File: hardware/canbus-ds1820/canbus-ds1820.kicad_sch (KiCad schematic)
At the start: 35 parts, among them J1 USB_B_Micro, J2 SWD, J3 UART, J4 3-pole terminal, J5 CANBus, J6 CANBus, Q1 2N7002, Q2 2N7002, Q3 BSS84, U1 MCP1754S-3302xCB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

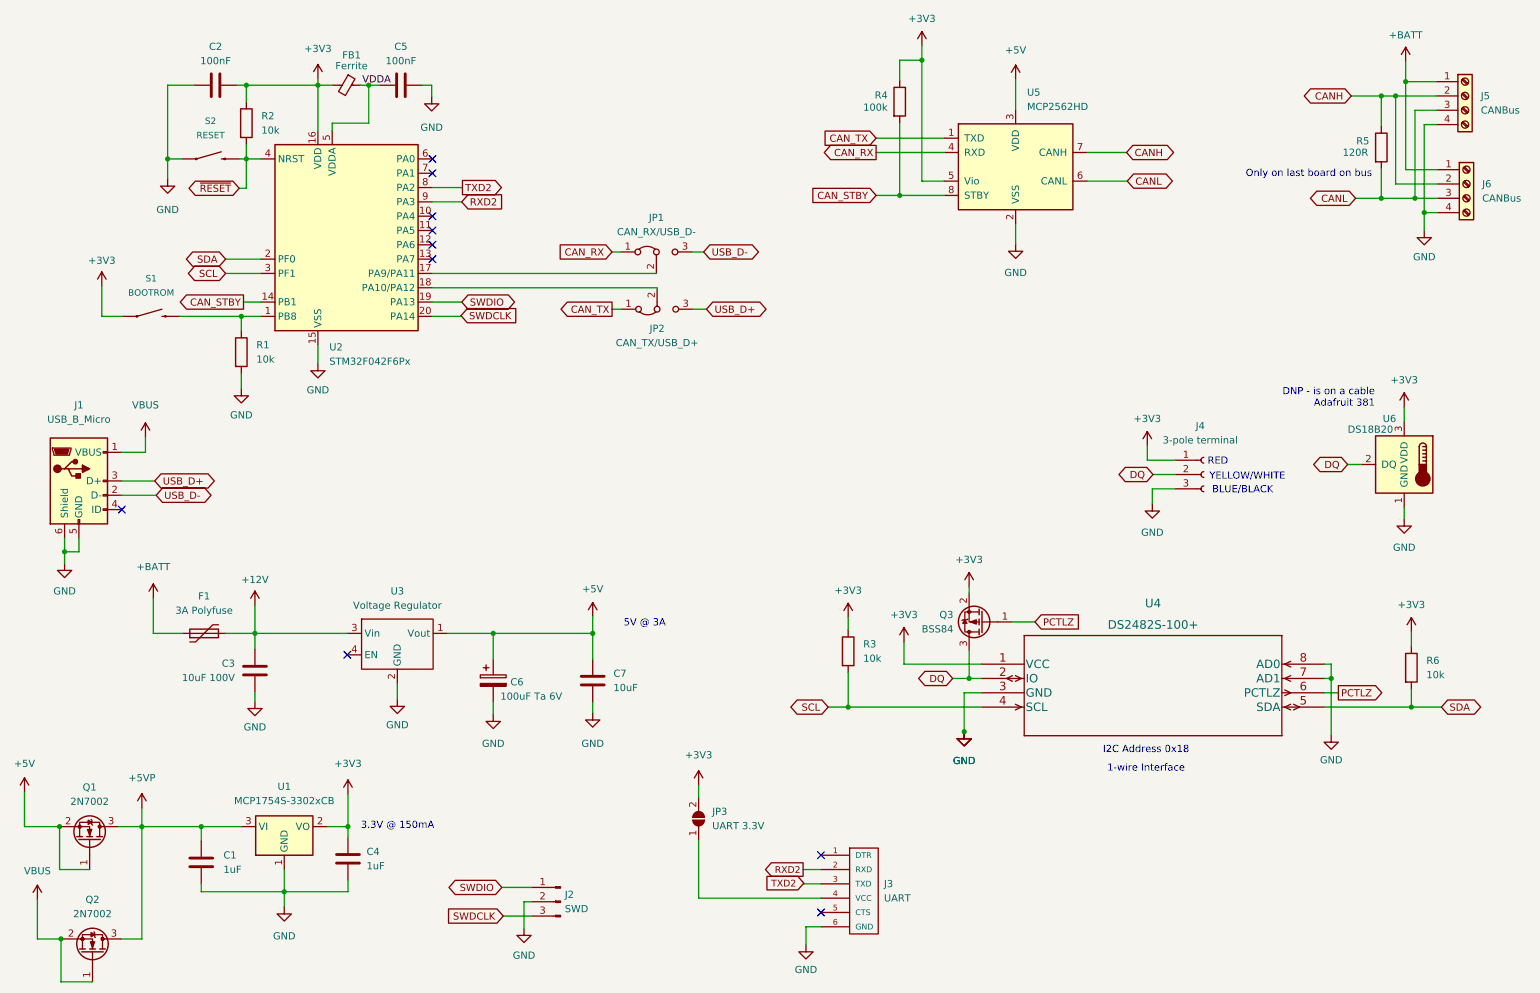
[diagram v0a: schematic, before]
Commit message: Implemented DS1820 directly, no DS2482
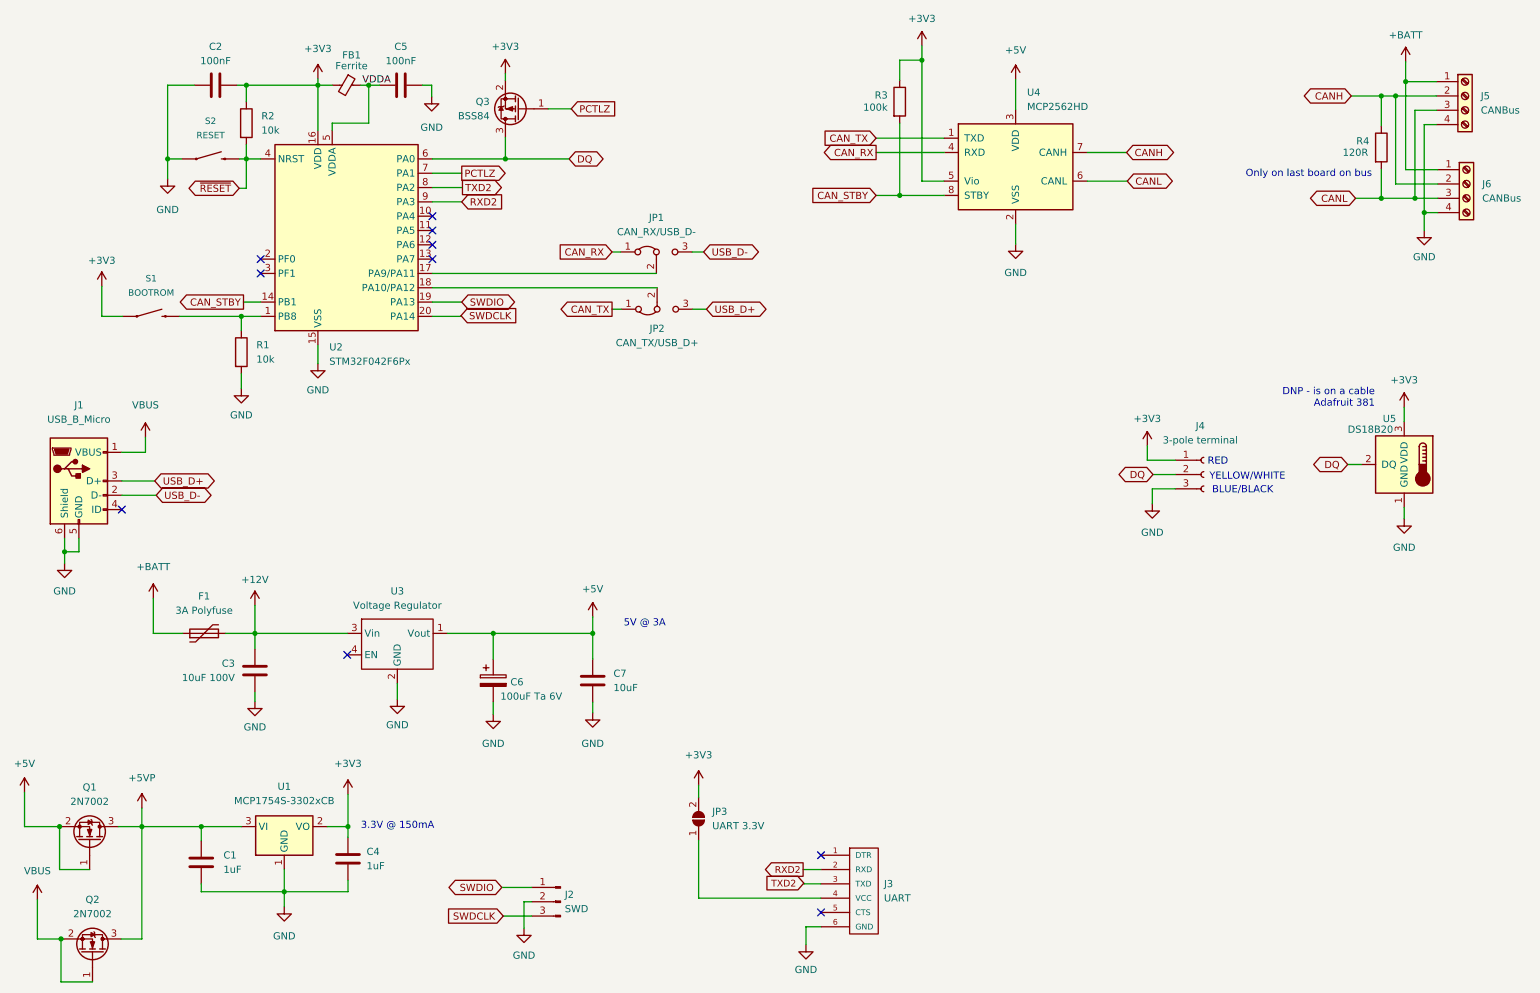
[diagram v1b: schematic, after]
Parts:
- removed R3, R6: 10k, Resistor_SMD:R_0805_2012Metric_Pad1.20x1.40mm_HandSolder, symbol Device:R
- removed U4: DS2482S-100+, UltraLibrarian:DS2482S-100&plus_, symbol UltraLibrarian:DS2482S-100+
- renumbered R4 to R3, R5 to R4, U5 to U4, U6 to U5
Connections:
- net DQ: now also U2.6 (PA0)
- net PCTLZ: now also U2.7 (PA1)
- net SCL: no longer names the net of U2.3 (PF1)
- net SDA: no longer names the net of U2.2 (PF0)
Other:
- note removed: "1-wire Interface"
- note removed: "I2C Address 0x18"
